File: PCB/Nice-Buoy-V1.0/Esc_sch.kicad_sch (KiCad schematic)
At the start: 0 parts

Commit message: Many changes in schematics
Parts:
- added J6: ESC-BB, Connector_JST:JST_XH_B3B-XH-A_1x03_P2.50mm_Vertical, symbol Connector:Conn_01x03_Pin
- added J7: ESC-SB, Connector_JST:JST_XH_B3B-XH-A_1x03_P2.50mm_Vertical, symbol Connector:Conn_01x03_Pin
- added R106 (x2): 100, A_Device:R_0603, symbol Device:R_Small
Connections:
- new net: J7.1 (Pin_1), R106.2
- new net: J6.1 (Pin_1), R106.2
- new net ESC_BB: R106.1
- new net ESC_SB: R106.1
- new net GND: J6.2 (Pin_2), J7.2 (Pin_2)
- no-connect marks 0 -> 2
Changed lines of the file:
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@@
 (kicad_sch (version 20230121) (generator eeschema)
   (paper "A4")
+  (no_connect (at 130.81 110.49))
+  (no_connect (at 130.81 87.63))
+  (wire (pts (xy 121.92 105.41) (xy 130.81 105.41))
+    (stroke (width 0) (type default))
+  )
+  (wire (pts (xy 106.68 82.55) (xy 116.84 82.55))
+    (stroke (width 0) (type default))
+  )
+  (wire (pts (xy 106.68 105.41) (xy 116.84 105.41))
+    (stroke (width 0) (type default))
+  )
+  (wire (pts (xy 121.92 82.55) (xy 130.81 82.55))
+    (stroke (width 0) (type default))
+  )
+  (wire (pts (xy 128.27 107.95) (xy 128.27 113.03))
+    (stroke (width 0) (type default))
+  )
+  (wire (pts (xy 128.27 85.09) (xy 128.27 90.17))
+    (stroke (width 0) (type default))
+  )
+  (wire (pts (xy 130.81 85.09) (xy 128.27 85.09))
+    (stroke (width 0) (type default))
+  )
+  (wire (pts (xy 130.81 107.95) (xy 128.27 107.95))
+    (stroke (width 0) (type default))
+  )
+  (hierarchical_label "ESC_BB" (shape output) (at 106.68 82.55 180) (fields_autoplaced)
+    (effects (font (size 1.27 1.27)) (justify right))
+  )
+  (hierarchical_label "ESC_SB" (shape output) (at 106.68 105.41 180) (fields_autoplaced)
+    (effects (font (size 1.27 1.27)) (justify right))
+  )
+  (symbol (lib_id "power:GND") (at 128.27 90.17 0) (unit 1)
+    (in_bom yes) (on_board yes) (dnp no) (fields_autoplaced)
+    (property "Reference" "#PWR027" (at 128.27 96.52 0)
+      (effects (font (size 1.27 1.27)) hide)
+    )
+    (property "Value" "GND" (at 128.27 95.25 0)
+      (effects (font (size 1.27 1.27)))
+    )
+    (property "Footprint" "" (at 128.27 90.17 0)
+      (effects (font (size 1.27 1.27)) hide)
+    )
+    (property "Datasheet" "" (at 128.27 90.17 0)
+      (effects (font (size 1.27 1.27)) hide)
+    )
+    (pin "1")
+    (instances
+      (project "Nice-Buoy-V1.0"
+        (path "/77bea089-a6ae-4a6f-b95b-7a9010ad7c5d/ca10023c-a303-42f5-abd0-839d0a1e9923"
+          (reference "#PWR027") (unit 1)
+        )
+      )
+    )
+  )
+  (symbol (lib_id "Connector:Conn_01x03_Pin") (at 135.89 107.95 0) (mirror y) (unit 1)
+    (in_bom yes) (on_board yes) (dnp no)
+    (property "Reference" "J7" (at 133.35 101.6 0)
+      (effects (font (size 1.27 1.27)))
+    )
+    (property "Value" "ESC-SB" (at 140.97 107.95 0)
+      (effects (font (size 1.27 1.27)))
+    )
+    (property "Footprint" "Connector_JST:JST_XH_B3B-XH-A_1x03_P2.50mm_Vertical" (at 135.89 107.95 0)
+      (effects (font (size 1.27 1.27)) hide)
+    )
+    (property "Datasheet" "~" (at 135.89 107.95 0)
+      (effects (font (size 1.27 1.27)) hide)
+    )
+    (property "LCSC" "C161870" (at 135.89 107.95 0)
+      (effects (font (size 1.27 1.27)) hide)
+    )
+    (pin "1")
+    (pin "2")
+    (pin "3")
+    (instances
+      (project "Nice-Buoy-V1.0"
+        (path "/77bea089-a6ae-4a6f-b95b-7a9010ad7c5d/ca10023c-a303-42f5-abd0-839d0a1e9923"
+          (reference "J7") (unit 1)
+        )
+      )
+    )
+  )
+  (symbol (lib_id "Device:R_Small") (at 119.38 82.55 90) (unit 1)
+    (in_bom yes) (on_board yes) (dnp no)
+    (property "Reference" "R106" (at 114.3 81.28 90)
+      (effects (font (size 1.27 1.27)))
+    )
+    (property "Value" "100" (at 119.38 85.09 90)
+      (effects (font (size 1.27 1.27)))
+    )
+    (property "Footprint" "A_Device:R_0603" (at 119.38 82.55 0)
+      (effects (font (size 1.27 1.27)) hide)
+    )
+    (property "Datasheet" "~" (at 119.38 82.55 0)
+      (effects (font (size 1.27 1.27)) hide)
+    )
+    (pin "1")
+    (pin "2")
+    (instances
+      (project "Nice-Buoy-V1.0"
+        (path "/77bea089-a6ae-4a6f-b95b-7a9010ad7c5d/b4716c37-6296-4cc3-83d4-c08b9373ace7"
+          (reference "R106") (unit 1)
+        )
+        (path "/77bea089-a6ae-4a6f-b95b-7a9010ad7c5d/015165a8-30a1-4680-bca0-c8d83aec4be2"
+          (reference "R5") (unit 1)
+        )
+        (path "/77bea089-a6ae-4a6f-b95b-7a9010ad7c5d/ca10023c-a303-42f5-abd0-839d0a1e9923"
+          (reference "R26") (unit 1)
+        )
+      )
+    )
+  )
+  (symbol (lib_id "Connector:Conn_01x03_Pin") (at 135.89 85.09 0) (mirror y) (unit 1)
+    (in_bom yes) (on_board yes) (dnp no)
+    (property "Reference" "J6" (at 133.35 78.74 0)
+      (effects (font (size 1.27 1.27)))
+    )
+    (property "Value" "ESC-BB" (at 140.97 85.09 0)
+      (effects (font (size 1.27 1.27)))
+    )
+    (property "Footprint" "Connector_JST:JST_XH_B3B-XH-A_1x03_P2.50mm_Vertical" (at 135.89 85.09 0)
+      (effects (font (size 1.27 1.27)) hide)
+    )
+    (property "Datasheet" "~" (at 135.89 85.09 0)
+      (effects (font (size 1.27 1.27)) hide)
+    )
+    (property "LCSC" "C161870" (at 135.89 85.09 0)
+      (effects (font (size 1.27 1.27)) hide)
+    )
+    (pin "1")
+    (pin "2")
+    (pin "3")
+    (instances
+      (project "Nice-Buoy-V1.0"
+        (path "/77bea089-a6ae-4a6f-b95b-7a9010ad7c5d/ca10023c-a303-42f5-abd0-839d0a1e9923"
+          (reference "J6") (unit 1)
+        )
+      )
+    )
+  )
+  (symbol (lib_id "Device:R_Small") (at 119.38 105.41 90) (unit 1)
+    (in_bom yes) (on_board yes) (dnp no)
+    (property "Reference" "R106" (at 114.3 104.14 90)
+      (effects (font (size 1.27 1.27)))
+    )
+    (property "Value" "100" (at 119.38 107.95 90)
+      (effects (font (size 1.27 1.27)))
+    )
+    (property "Footprint" "A_Device:R_0603" (at 119.38 105.41 0)
+      (effects (font (size 1.27 1.27)) hide)
+    )
+    (property "Datasheet" "~" (at 119.38 105.41 0)
+      (effects (font (size 1.27 1.27)) hide)
+    )
+    (pin "1")
+    (pin "2")
+    (instances
+      (project "Nice-Buoy-V1.0"
+        (path "/77bea089-a6ae-4a6f-b95b-7a9010ad7c5d/b4716c37-6296-4cc3-83d4-c08b9373ace7"
+          (reference "R106") (unit 1)
+        )
+        (path "/77bea089-a6ae-4a6f-b95b-7a9010ad7c5d/015165a8-30a1-4680-bca0-c8d83aec4be2"
+          (reference "R5") (unit 1)
+        )
+        (path "/77bea089-a6ae-4a6f-b95b-7a9010ad7c5d/ca10023c-a303-42f5-abd0-839d0a1e9923"
+          (reference "R27") (unit 1)
+        )
+      )
+    )
+  )
+  (symbol (lib_id "power:GND") (at 128.27 113.03 0) (unit 1)
+    (in_bom yes) (on_board yes) (dnp no) (fields_autoplaced)
+    (property "Reference" "#PWR028" (at 128.27 119.38 0)
+      (effects (font (size 1.27 1.27)) hide)
+    )
+    (property "Value" "GND" (at 128.27 118.11 0)
+      (effects (font (size 1.27 1.27)))
+    )
+    (property "Footprint" "" (at 128.27 113.03 0)
+      (effects (font (size 1.27 1.27)) hide)
+    )
+    (property "Datasheet" "" (at 128.27 113.03 0)
+      (effects (font (size 1.27 1.27)) hide)
+    )
+    (pin "1")
+    (instances
+      (project "Nice-Buoy-V1.0"
+        (path "/77bea089-a6ae-4a6f-b95b-7a9010ad7c5d/ca10023c-a303-42f5-abd0-839d0a1e9923"
+          (reference "#PWR028") (unit 1)
+        )
+      )
+    )
+  )
 )

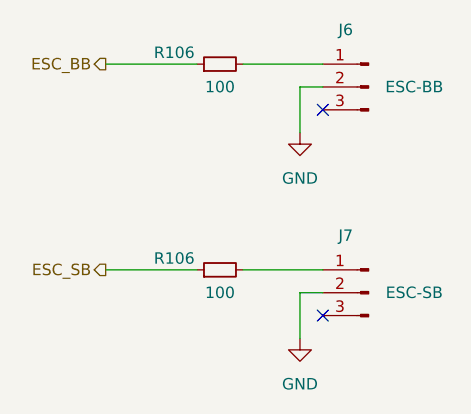
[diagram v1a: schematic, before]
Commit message: Battery monitor not working
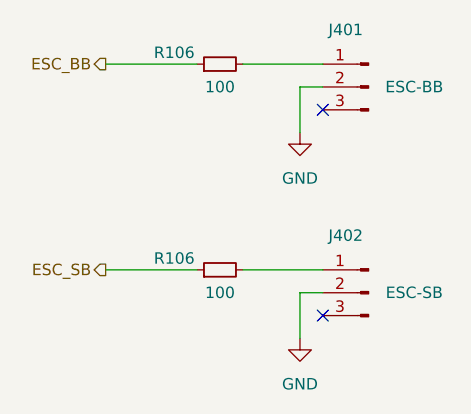
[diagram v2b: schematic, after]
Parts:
- renumbered J6 to J401, J7 to J402
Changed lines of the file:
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@@
   (symbol (lib_id "power:GND") (at 128.27 90.17 0) (unit 1)
     (in_bom yes) (on_board yes) (dnp no) (fields_autoplaced)
-    (property "Reference" "#PWR027" (at 128.27 96.52 0)
+    (property "Reference" "#PWR0401" (at 128.27 96.52 0)
       (effects (font (size 1.27 1.27)) hide)
     )
@@
       (project "Nice-Buoy-V1.0"
         (path "/77bea089-a6ae-4a6f-b95b-7a9010ad7c5d/ca10023c-a303-42f5-abd0-839d0a1e9923"
-          (reference "#PWR027") (unit 1)
+          (reference "#PWR0401") (unit 1)
         )
       )
@@
   (symbol (lib_id "Connector:Conn_01x03_Pin") (at 135.89 107.95 0) (mirror y) (unit 1)
     (in_bom yes) (on_board yes) (dnp no)
-    (property "Reference" "J7" (at 133.35 101.6 0)
+    (property "Reference" "J402" (at 133.35 101.6 0)
       (effects (font (size 1.27 1.27)))
     )
@@
       (project "Nice-Buoy-V1.0"
         (path "/77bea089-a6ae-4a6f-b95b-7a9010ad7c5d/ca10023c-a303-42f5-abd0-839d0a1e9923"
-          (reference "J7") (unit 1)
+          (reference "J402") (unit 1)
         )
       )
@@
         )
         (path "/77bea089-a6ae-4a6f-b95b-7a9010ad7c5d/ca10023c-a303-42f5-abd0-839d0a1e9923"
-          (reference "R26") (unit 1)
+          (reference "R401") (unit 1)
         )
       )
@@
   (symbol (lib_id "Connector:Conn_01x03_Pin") (at 135.89 85.09 0) (mirror y) (unit 1)
     (in_bom yes) (on_board yes) (dnp no)
-    (property "Reference" "J6" (at 133.35 78.74 0)
+    (property "Reference" "J401" (at 133.35 78.74 0)
       (effects (font (size 1.27 1.27)))
     )
@@
       (project "Nice-Buoy-V1.0"
         (path "/77bea089-a6ae-4a6f-b95b-7a9010ad7c5d/ca10023c-a303-42f5-abd0-839d0a1e9923"
-          (reference "J6") (unit 1)
+          (reference "J401") (unit 1)
         )
       )
@@
         )
         (path "/77bea089-a6ae-4a6f-b95b-7a9010ad7c5d/ca10023c-a303-42f5-abd0-839d0a1e9923"
-          (reference "R27") (unit 1)
+          (reference "R402") (unit 1)
         )
       )
@@
   (symbol (lib_id "power:GND") (at 128.27 113.03 0) (unit 1)
     (in_bom yes) (on_board yes) (dnp no) (fields_autoplaced)
-    (property "Reference" "#PWR028" (at 128.27 119.38 0)
+    (property "Reference" "#PWR0402" (at 128.27 119.38 0)
       (effects (font (size 1.27 1.27)) hide)
     )
@@
       (project "Nice-Buoy-V1.0"
         (path "/77bea089-a6ae-4a6f-b95b-7a9010ad7c5d/ca10023c-a303-42f5-abd0-839d0a1e9923"
-          (reference "#PWR028") (unit 1)
+          (reference "#PWR0402") (unit 1)
         )
       )
